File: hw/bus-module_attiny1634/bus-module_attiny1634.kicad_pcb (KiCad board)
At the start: 2 copper layers, 27.3 x 48 mm, 37 parts, among them J1 CONN_5X2, J2 CONN_5X2, J3 CONN-ISP-6, J4 CONN_1, J5 CONN_1, J6 CONN_1, J7 CONN_1, U1 7,3728MHz, U2 25LCXXX, U3 ATTINY1634-SOIC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

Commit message: R2, R3, R4 100 Ohms
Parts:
- R2, R3, R4: value 1k -> 100
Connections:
- D2 pad 2: (no net) -> Net-(D2-Pad2)
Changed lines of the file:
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@@
-(kicad_pcb (version 20171130) (host pcbnew 5.0.0-fee4fd1~66~ubuntu16.04.1)
+(kicad_pcb (version 20171130) (host pcbnew 5.0.2-bee76a0~70~ubuntu18.04.1)
   (general
     (thickness 1.6)
@@
     (zones 0)
     (modules 37)
-    (nets 30)
+    (nets 31)
   )
   (page A4)
@@
     (pad_drill 2.5)
     (pad_to_mask_clearance 0)
+    (solder_mask_min_width 0.25)
     (aux_axis_origin 0 0)
     (grid_origin 89.4 83.32)
@@
   (net 28 "Net-(F1-Pad1)")
   (net 29 VCC)
+  (net 30 "Net-(D2-Pad2)")
   (net_class Default "This is the default net class."
     (clearance 0.2)
@@
     (add_net "Net-(C2-Pad1)")
     (add_net "Net-(C3-Pad1)")
+    (add_net "Net-(D2-Pad2)")
     (add_net "Net-(F1-Pad1)")
     (add_net "Net-(R1-Pad2)")
@@
     (pad 3 smd rect (at 0.95 -0.95 90) (size 0.85 0.85) (layers F.Cu F.Paste F.Mask)
       (net 27 /B))
-    (pad 2 smd rect (at 0.95 0.95 90) (size 0.85 0.85) (layers F.Cu F.Paste F.Mask))
+    (pad 2 smd rect (at 0.95 0.95 90) (size 0.85 0.85) (layers F.Cu F.Paste F.Mask)
+      (net 30 "Net-(D2-Pad2)"))
     (pad 1 smd rect (at -0.76962 0.95 90) (size 1.2 0.85) (layers F.Cu F.Paste F.Mask)
       (net 1 GND))
@@
       (effects (font (size 0.8 0.8) (thickness 0.15)))
     )
-    (fp_text value 1k (at 0.127 1.524 270) (layer F.Fab)
+    (fp_text value 100 (at 0.127 1.524 270) (layer F.Fab)
       (effects (font (size 0.8 0.8) (thickness 0.15)))
     )
@@
       (effects (font (size 0.8 0.8) (thickness 0.15)))
     )
-    (fp_text value 1k (at 0.127 1.524 270) (layer F.Fab)
+    (fp_text value 100 (at 0.127 1.524 270) (layer F.Fab)
       (effects (font (size 0.8 0.8) (thickness 0.15)))
     )
@@
       (effects (font (size 0.8 0.8) (thickness 0.15)))
     )
-    (fp_text value 1k (at 0.127 1.524 270) (layer F.Fab)
+    (fp_text value 100 (at 0.127 1.524 270) (layer F.Fab)
       (effects (font (size 0.8 0.8) (thickness 0.15)))
     )
@@
   (gr_line (start 85 86) (end 80 86) (angle 90) (layer Cmts.User) (width 0.1))
   (gr_circle (center 99.492 100.254) (end 100.492 100.254) (layer Cmts.User) (width 0.2))
+  (segment (start 102.386501 106.341497) (end 102.031999 106.695999) (width 0.3) (layer F.Cu) (net 0) (status 30))
   (segment (start 94.48 89.289) (end 94.48 87.384) (width 0.6) (layer F.Cu) (net 1) (status 10))
   (segment (start 95.496 86.368) (end 95.496 83.32) (width 0.6) (layer F.Cu) (net 1) (status 20))
@@
   (segment (start 93.9085 106.1165) (end 93.972 106.18) (width 0.8) (layer F.Cu) (net 1))
   (via (at 93.972 106.18) (size 0.8) (drill 0.4) (layers F.Cu B.Cu) (net 1))
-  (segment (start 103.37 98.941) (end 103.37 99.322) (width 0.3) (layer F.Cu) (net 7) (status 30))
-  (segment (start 102.386501 106.341497) (end 102.031999 106.695999) (width 0.3) (layer F.Cu) (net 0) (status 30))
   (segment (start 97.02 88.9715) (end 97.02 89.289) (width 0.3) (layer F.Cu) (net 2) (status 30))
   (segment (start 97.635999 88.355501) (end 97.02 88.9715) (width 0.3) (layer F.Cu) (net 2) (status 20))
@@
   (segment (start 104.386002 82.049998) (end 104.386002 85.7965) (width 0.3) (layer B.Cu) (net 6))
   (segment (start 102.1 89.289) (end 102.1 88.082502) (width 0.3) (layer F.Cu) (net 6) (status 10))
+  (segment (start 103.37 98.941) (end 103.37 99.322) (width 0.3) (layer F.Cu) (net 7) (status 30))
   (segment (start 102.608 104.329878) (end 100.583989 106.353889) (width 0.3) (layer F.Cu) (net 7))
   (segment (start 100.583989 109.489987) (end 101.401502 110.3075) (width 0.3) (layer F.Cu) (net 7))

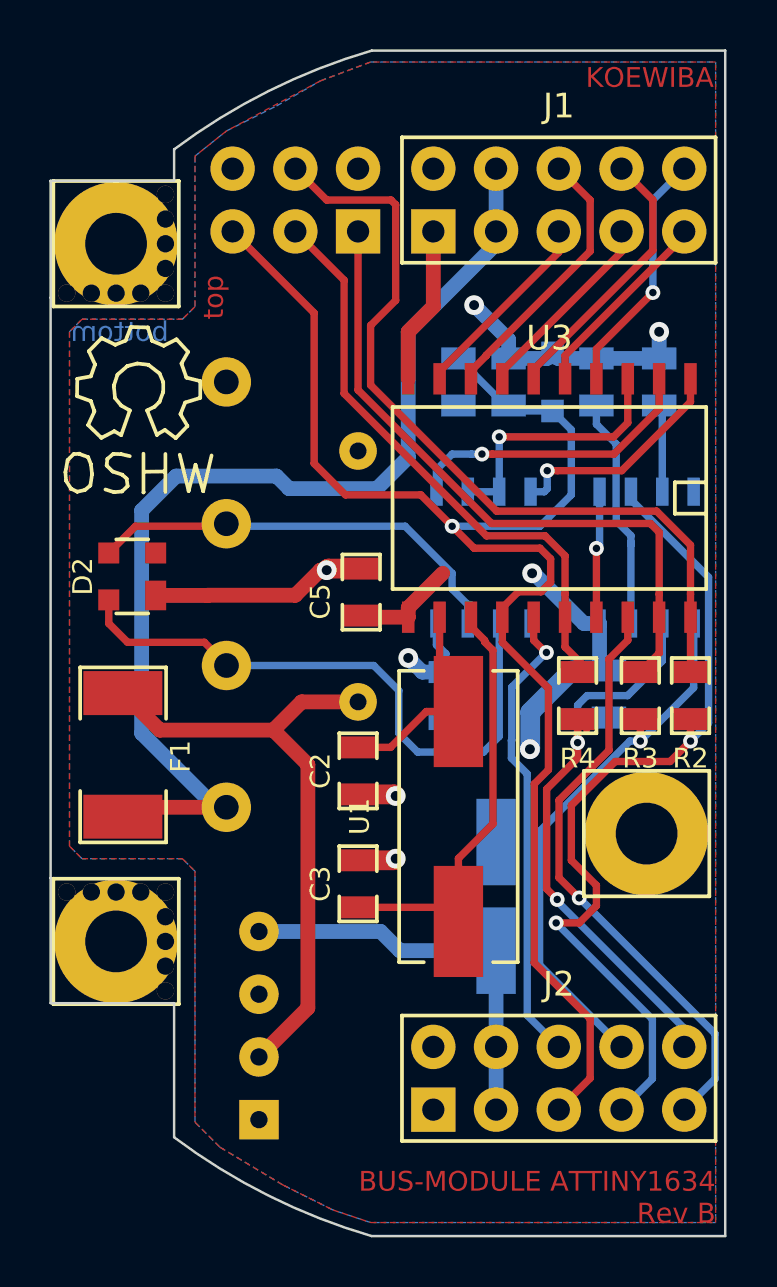
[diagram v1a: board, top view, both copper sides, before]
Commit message: Increase WAGO hole diameter, replace ELKO with keramic capacitor, Increase WAGO hole diameter, update footprints, update footprints, set Rev to C
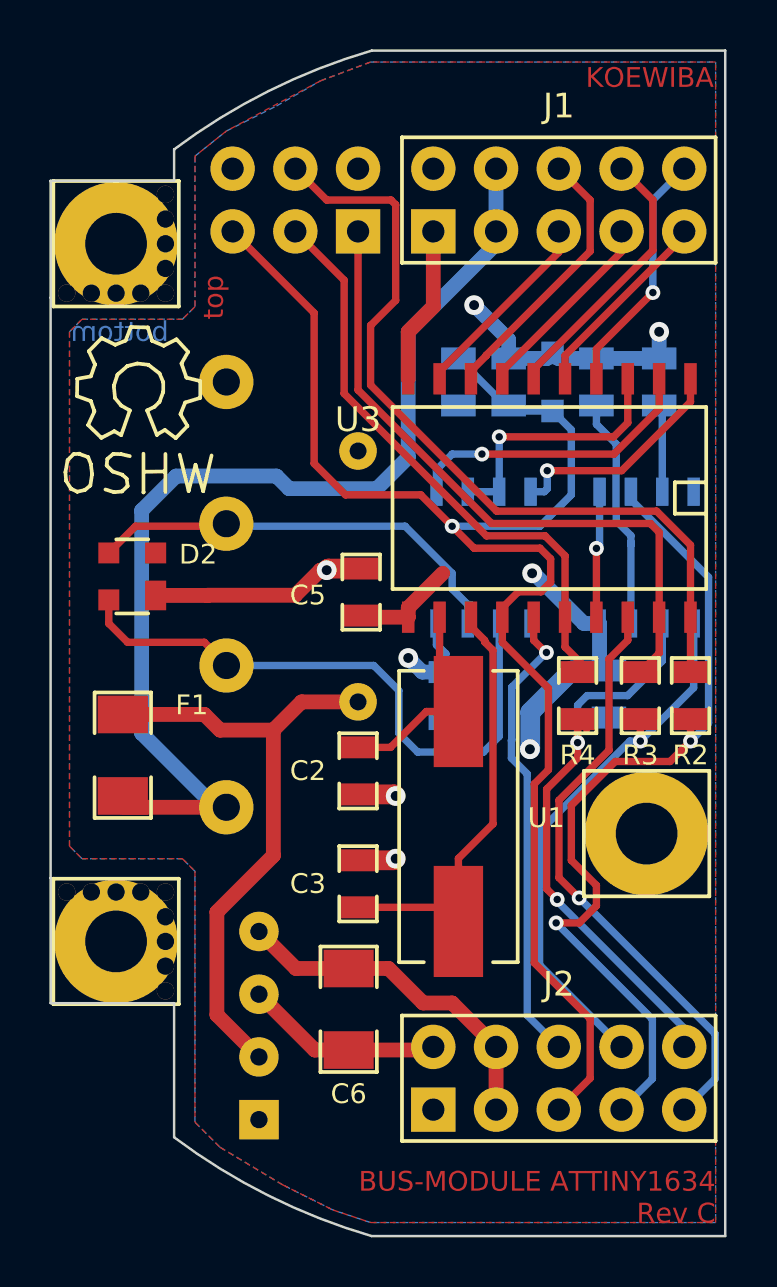
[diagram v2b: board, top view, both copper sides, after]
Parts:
- C6: value 100µF -> 100µF/6,3V VS; footprint Capacitors_SMD:CP_D6.3mm -> Capacitors_SMD:C_1206; moved to F.Cu
- F1: footprint Resistor:R_1812 -> Resistor:R_1206
- moved C6 7.52 mm to (92.1, 114.8), turned to 270 degrees
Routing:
- net GND: track 19.9 -> 27.9 mm
- net VCC: track 45.0 -> 43.7 mm
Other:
- board text added: "BUS-MODULE ATTINY1634 Rev C"
- board text added: "BUS-MODULE ATTINY1634 RevC"
- board text removed: "BUS-MODULE ATTINY1634 Rev B"
- board text removed: "BUS-MODULE ATTINY1634 RevB"

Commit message: Update to KiCAD6: bus-module_attiny1634
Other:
- net class Default removed
- net class Power removed
